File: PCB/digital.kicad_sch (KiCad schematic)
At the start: 29 parts, among them J3 JTAG, J4 ICSP, J8 RFID_COAX, U2 PIC32MK0256MCJ048-I/Y8X, U3 TCAN334D, Y1 ECS-3225SMV-080-GP-TR, Y2 ECS-3225SMV-080-GP-TR

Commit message: sparse changes
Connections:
- net UART_CTS renamed /UART_CTS
- net UART_RTS renamed UART_CLK
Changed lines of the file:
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@@
     (stroke (width 0) (type default))
   )
-  (wire (pts (xy 72.39 73.66) (xy 85.09 73.66))
+  (wire (pts (xy 71.12 73.66) (xy 85.09 73.66))
     (stroke (width 0) (type default))
   )
@@
     (stroke (width 0) (type default))
   )
-  (wire (pts (xy 63.5 80.01) (xy 72.39 80.01))
+  (wire (pts (xy 63.5 80.01) (xy 71.12 80.01))
     (stroke (width 0) (type default))
   )
@@
     (stroke (width 0) (type default))
   )
-  (wire (pts (xy 72.39 80.01) (xy 72.39 73.66))
+  (wire (pts (xy 71.12 80.01) (xy 71.12 73.66))
     (stroke (width 0) (type default))
   )
@@
     )
   )
-  (global_label "UART_CTS" (shape input) (at 85.09 81.28 180) (fields_autoplaced)
-    (effects (font (size 1.27 1.27)) (justify right))
-    (property "Intersheetrefs" "${INTERSHEET_REFS}" (at 73.1128 81.28 0)
+  (global_label "{slash}UART_CTS" (shape input) (at 85.09 81.28 180) (fields_autoplaced)
+    (effects (font (size 1.27 1.27)) (justify right))
+    (property "Intersheetrefs" "${INTERSHEET_REFS}" (at 71.7029 81.28 0)
       (effects (font (size 1.27 1.27)) (justify right) hide)
     )
@@
     )
   )
-  (global_label "UART_RTS" (shape input) (at 85.09 83.82 180) (fields_autoplaced)
-    (effects (font (size 1.27 1.27)) (justify right))
-    (property "Intersheetrefs" "${INTERSHEET_REFS}" (at 73.1128 83.82 0)
-      (effects (font (size 1.27 1.27)) (justify right) hide)
-    )
+  (global_label "UART_CLK" (shape input) (at 85.09 83.82 180) (fields_autoplaced)
+    (effects (font (size 1.27 1.27)) (justify right))
+    (property "Intersheetrefs" "${INTERSHEET_REFS}" (at 72.9124 83.82 0)
+      (effects (font (size 1.27 1.27)) (justify right) hide)
+    )

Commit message: change file structure
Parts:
- added J11: USART, symbol Connector:DE9_Plug
- added J14: FINAL_CARRERA_UP, symbol Connector_Generic:Conn_01x03
- added J15: FINAL_CARRERA_DOWN, symbol Connector_Generic:Conn_01x03
- added J7: SPI, symbol Connector_Generic:Conn_01x04
- added J9: CAN, symbol Connector:DE9_Plug
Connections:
- net +3.3V: now also J14.1 (Pin_1), J15.1 (Pin_1), J9.9
- net CANH: now also J9.7
- net CANL: now also J9.2
- net GND: now also J11.5, J14.3 (Pin_3), J15.3 (Pin_3), J9.3, J9.6
- net SPI_CK: now also J7.1 (Pin_1)
- net SPI_SDI: now also J7.2 (Pin_2)
- net SPI_SDO: now also J7.3 (Pin_3)
- net SPI_SS: now also J7.4 (Pin_4)
- net UART_CLK: now also J11.7
- net UART_RX: now also J11.2
- net UART_TX: now also J11.3
- net /UART_CTS: now also J11.8
- new net FINAL_CARRERA_DOWN: J15.2 (Pin_2)
- new net FINAL_CARRERA_UP: J14.2 (Pin_2)
- no-connect marks 8 -> 16
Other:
- note added: "5.- Shield (optional)"
- note added: "FINAL DE CARRERA"
- note added: "SPI + USART"
- moved on the sheet: C28, C29, J3, J4, J8, JP2, R8, U3, U6

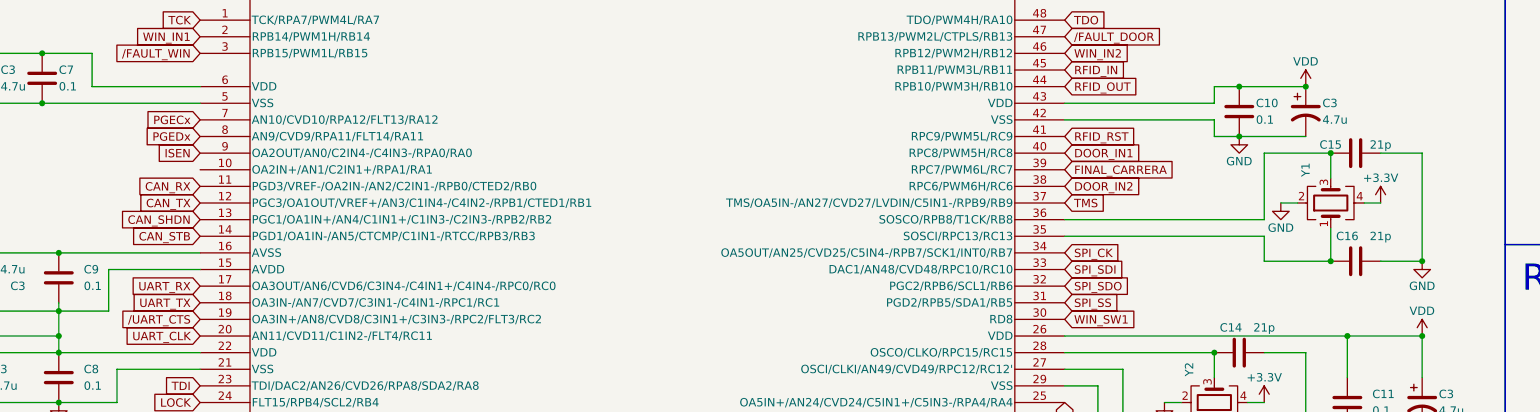
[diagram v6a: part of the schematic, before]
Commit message: changed to DCDC 3.3V, added extra bit for window ctrl + misc corrections
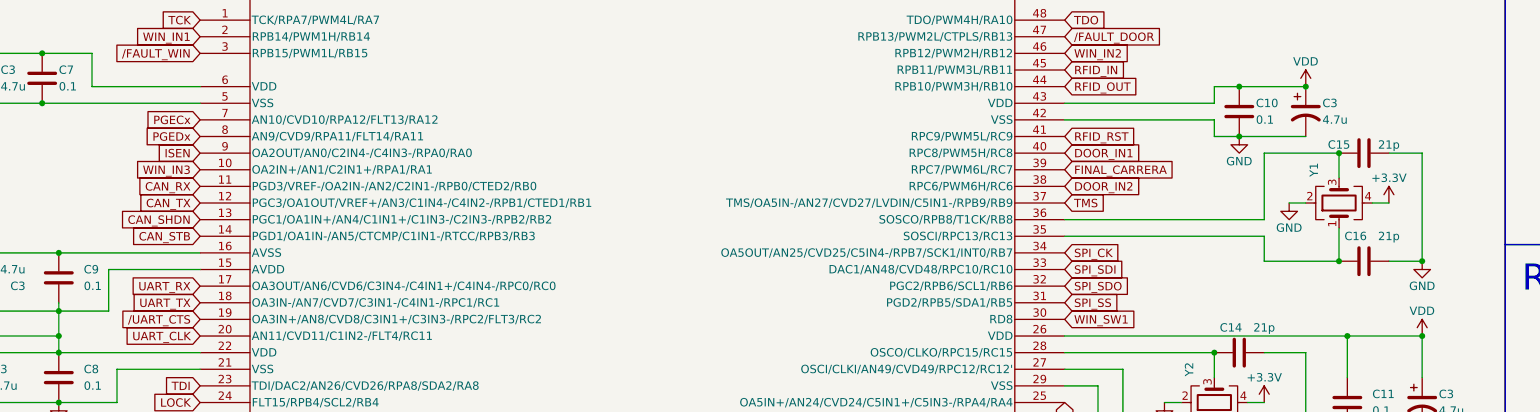
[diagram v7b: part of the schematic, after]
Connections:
- net WIN_IN3: now reaches U2.10 (OA2IN+/AN1/C2IN1+/RPA1/RA1)
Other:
- moved on the sheet: C15, C16, Y1

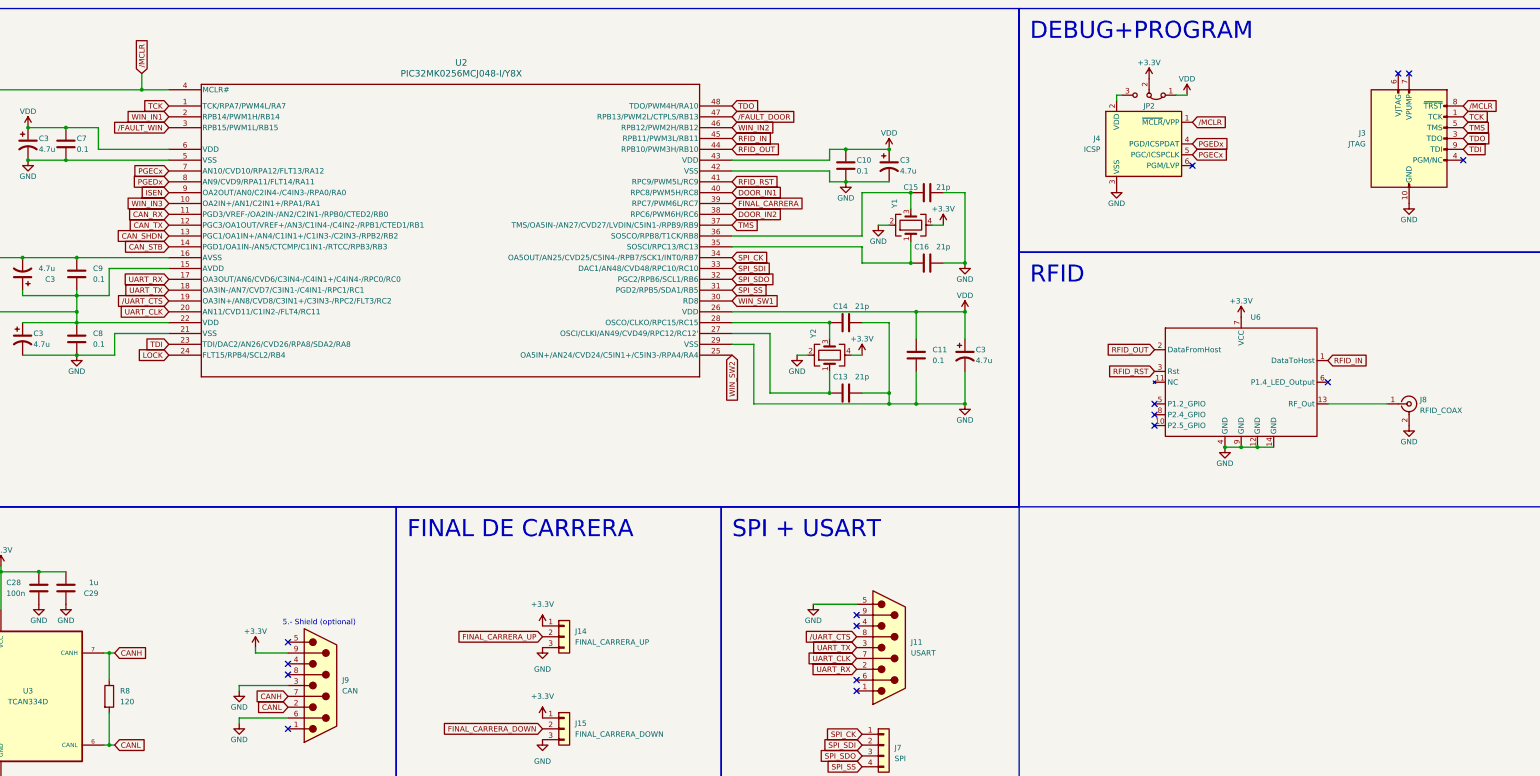
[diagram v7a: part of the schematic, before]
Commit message: added all components
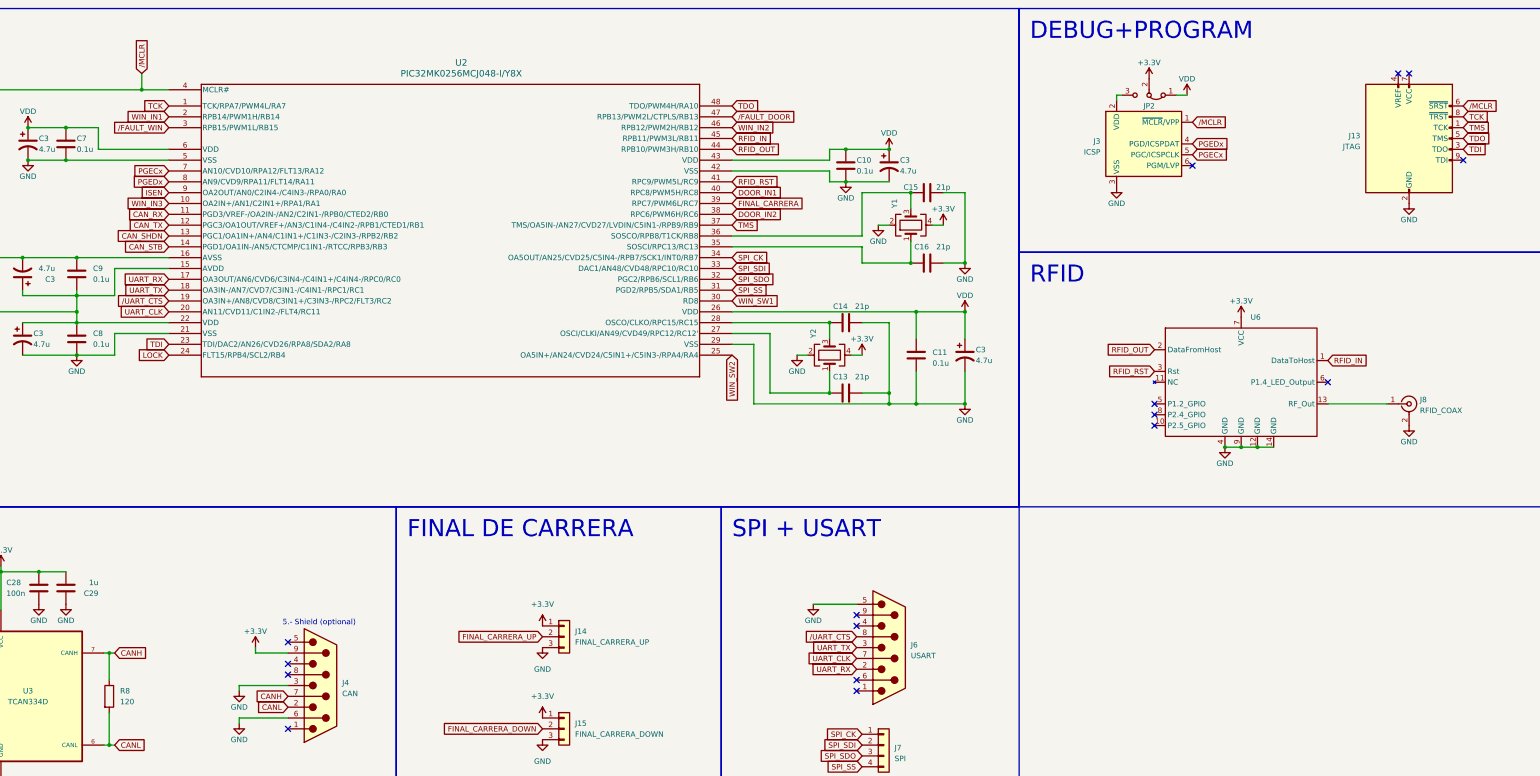
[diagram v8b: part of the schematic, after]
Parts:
- removed J11: USART, symbol Connector:DE9_Plug
- removed J3: JTAG, symbol Connector:Microsemi_FlashPro-JTAG-10
- removed J4: ICSP, symbol Connector:Conn_PIC_ICSP_ICD
- removed J9: CAN, symbol Connector:DE9_Plug
- added J13: JTAG, Connector_IDC:IDC-Header_2x05_P2.54mm_Vertical, symbol Connector:AVR-JTAG-10
- added J3: ICSP, Connector_PinHeader_2.54mm:PinHeader_1x06_P2.54mm_Vertical, symbol Connector:Conn_PIC_ICSP_ICD
- added J4: CAN, Connector_Dsub:DSUB-9_Male_Horizontal_P2.77x2.84mm_EdgePinOffset4.94mm_Housed_MountingHolesOffset7.48mm, symbol Connector:DE9_Plug
- added J6: USART, Connector_Dsub:DSUB-9_Male_Horizontal_P2.77x2.84mm_EdgePinOffset4.94mm_Housed_MountingHolesOffset7.48mm, symbol Connector:DE9_Plug
- C10, C11, C7, C8, C9: value 0.1 -> 0.1u; footprint (none) -> Capacitor_SMD:C_0805_2012Metric
- C12, C28, C29: footprint (none) -> Capacitor_SMD:C_0805_2012Metric
- C13, C14, C15, C16: footprint (none) -> Capacitor_SMD:C_01005_0402Metric
- C3: footprint (none) -> kicad_models:CAPAE430X550N
- J14, J15: footprint (none) -> TerminalBlock_MetzConnect:TerminalBlock_MetzConnect_Type011_RT05503HBWC_1x03_P5.00mm_Horizontal
- J7: footprint (none) -> TerminalBlock_MetzConnect:TerminalBlock_MetzConnect_Type011_RT05504HBWC_1x04_P5.00mm_Horizontal
- J8: footprint (none) -> Connector_Coaxial:BNC_TEConnectivity_1478035_Horizontal
- JP2: footprint (none) -> Connector_PinHeader_1.00mm:PinHeader_1x03_P1.00mm_Vertical
- R3, R4, R8: footprint (none) -> Resistor_SMD:R_0805_2012Metric
- U2: footprint TQFP48_Y8X_MCH -> kicad_models:PIC32MK0256MCJ048-I-Y8X_MCH
- U3: footprint (none) -> kicad_models:TCAN3413DR
- U6: footprint (none) -> DLP-RFID2:DLP-RFID2
- Y1, Y2: footprint ECS-3225SMV-080-GP-TR:OSC_ECS-3225SMV-080-GP-TR -> kicad_models:OSC_ECS-3225SMV-080-GP-TR
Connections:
- net +3.3V: now also J4.9
- net CANH: now also J4.7
- net CANL: now also J4.2
- net GND: now also J13.10 (GND), J13.2 (GND), J3.3 (VSS), J4.3, J4.6, J6.5
- net PGECx: now also J3.5 (PGC/ICSPCLK)
- net PGEDx: now also J3.4 (PGD/ICSPDAT)
- net TCK: now also J13.8 (~{TRST})
- net TDI: now also J13.3 (TDO)
- net TDO: now also J13.5 (TMS)
- net TMS: now also J13.1 (TCK)
- net UART_CLK: now also J6.7
- net UART_RX: now also J6.2
- net UART_TX: now also J6.3
- net /MCLR: now also J13.6 (~{SRST}), J3.1 (~{MCLR}/VPP)
- net /UART_CTS: now also J6.8
- net at JP2.3 (B): now also J3.2 (VDD)
